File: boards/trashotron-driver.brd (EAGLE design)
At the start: 76.2 x 76.2 mm, 17 parts, among them IC1 2967-MP6500, IC2 2967-MP6500, IC3 2967-MP6500, J4 455-1750-1-ND, J6 455-1750-1-ND, J9 455-1750-1-ND, U2 LM358

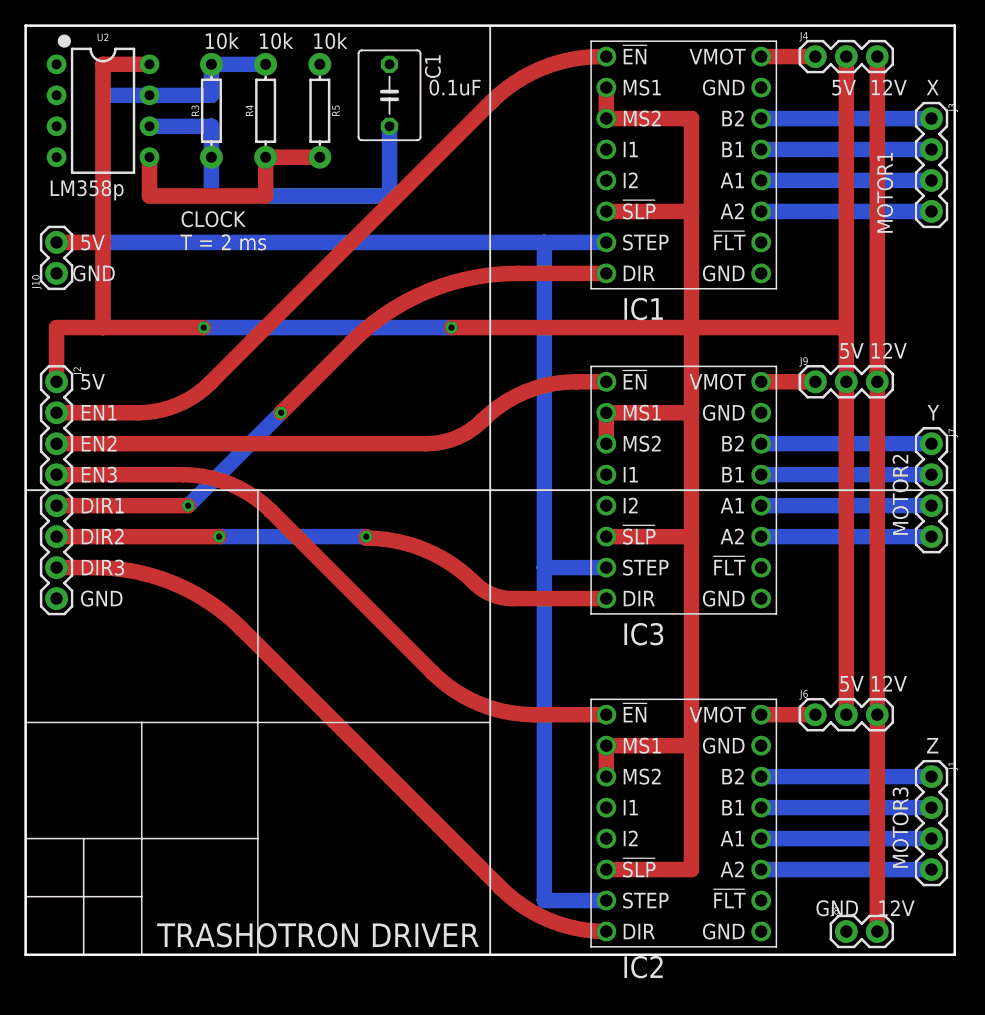
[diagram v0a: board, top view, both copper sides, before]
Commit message: this version of the boards is now all tested out on solderless breadboard
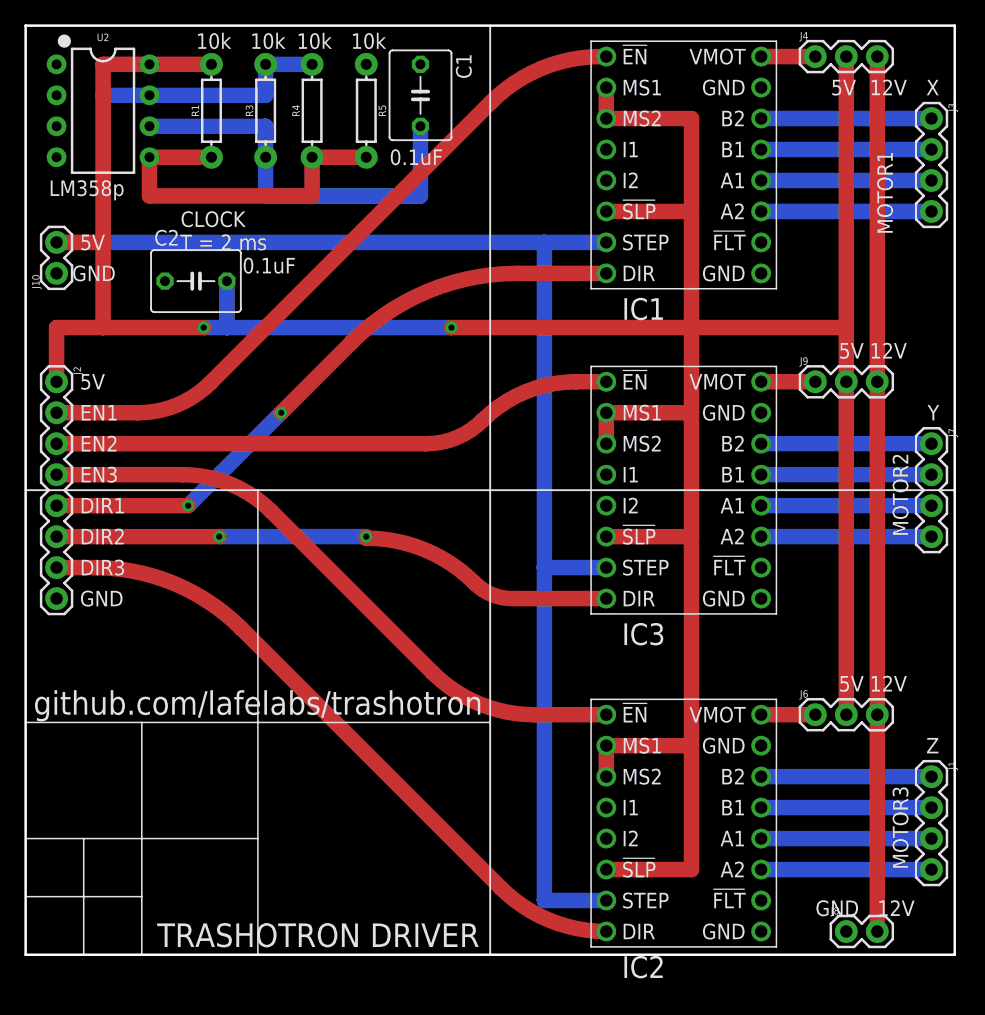
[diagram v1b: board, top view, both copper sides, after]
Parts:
- added C2: (no value), rcl:C050-050X075
- added R1: (no value), SparkFun-Resistors:AXIAL-0.3
- moved R3 4.44 mm to (19.7, 69.2)
- moved R4 3.81 mm to (23.5, 69.2)
- moved R5 3.81 mm to (27.9, 69.2)
- moved C1 2.54 mm to (32.4, 70.5)
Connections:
- net 5V: now also C2.2, R1.P$2
- net GND: now also C2.1
- net N$19: now also R1.P$1
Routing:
- net N$19: track 20.3 -> 29.2 mm
- net 5V: track 263.5 -> 272.4 mm
- net CLOCK: track 133.3 -> 137.2 mm
- net N$18: track 31.1 -> 33.7 mm
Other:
- board text added: "github.com/lafelabs/trashotron"
